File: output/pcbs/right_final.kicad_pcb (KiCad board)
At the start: 2 copper layers, 137 x 129 mm, 79 parts

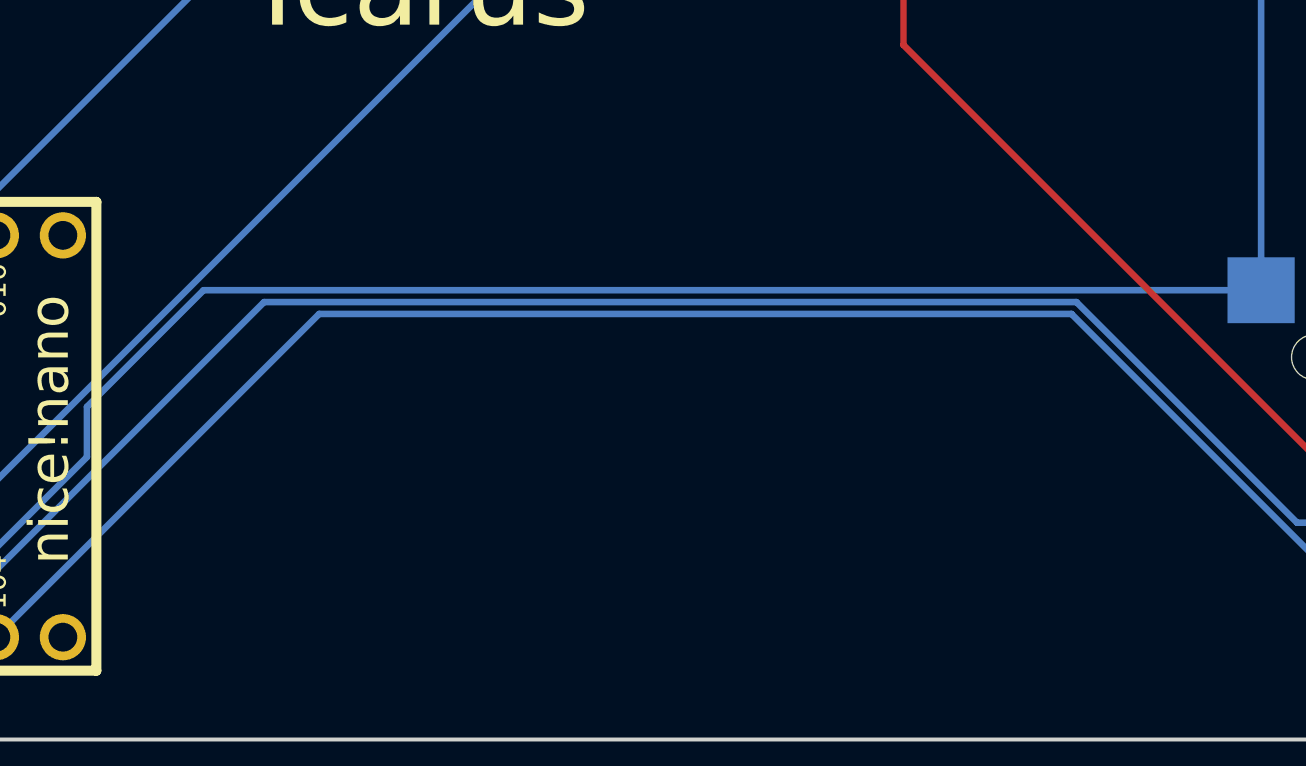
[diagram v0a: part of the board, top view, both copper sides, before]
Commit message: redesign for short board, left but no right pcb. Final pcbs for old design
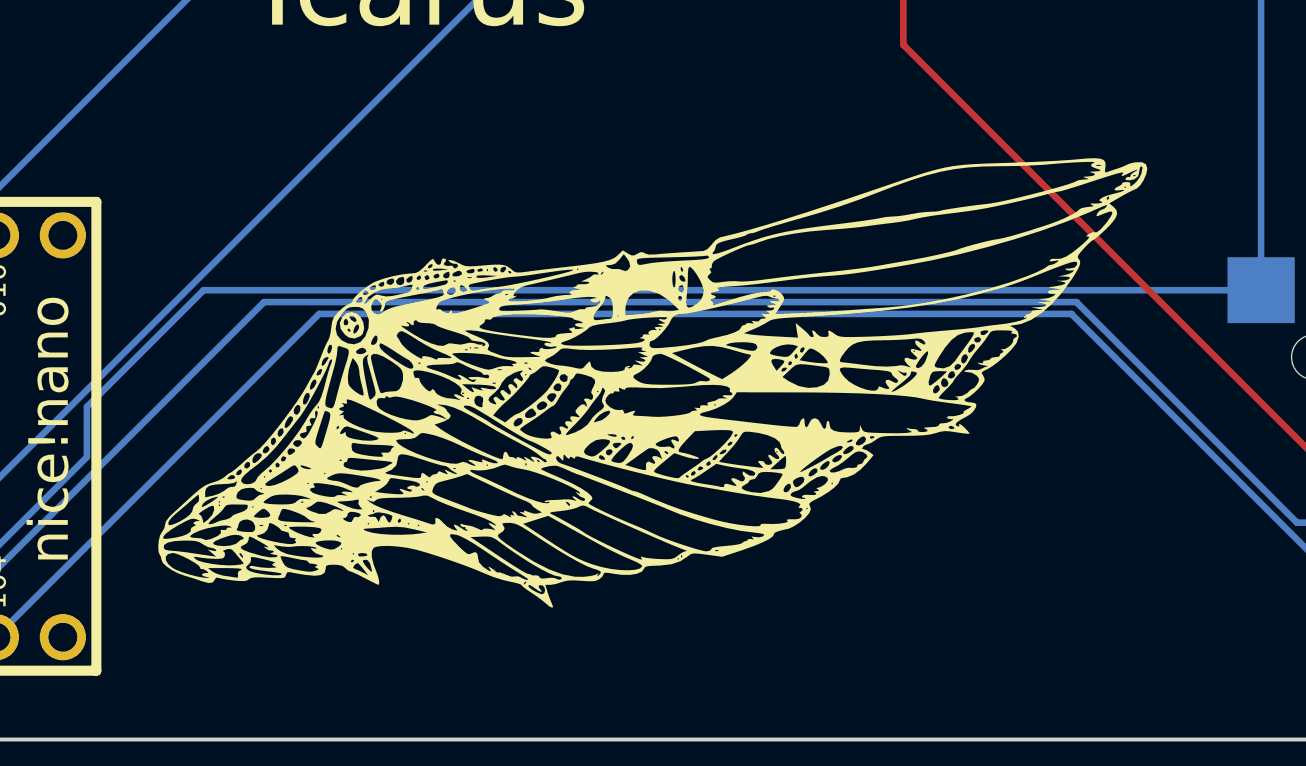
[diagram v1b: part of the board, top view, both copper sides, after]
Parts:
- added G***: LOGO, right_wing, F.Cu at (298.0, 198.2)
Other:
- rule pad_to_mask_clearance: 0.05 -> 0
